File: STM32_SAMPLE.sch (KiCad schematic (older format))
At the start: 19 parts

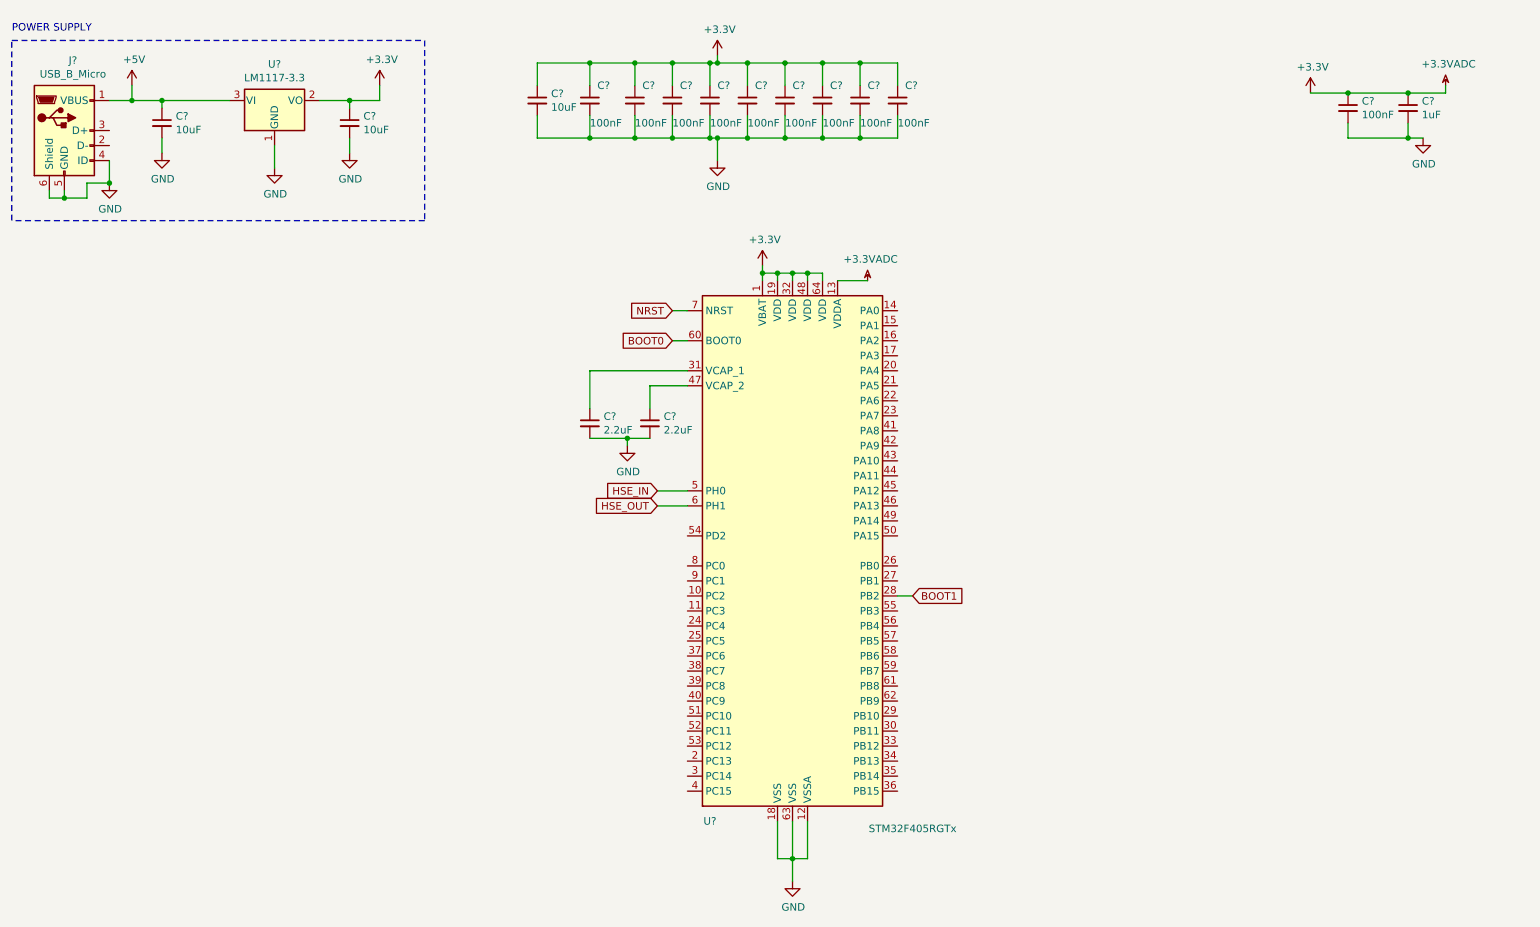
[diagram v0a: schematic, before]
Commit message: STM32 board bare minimum with HSI clock
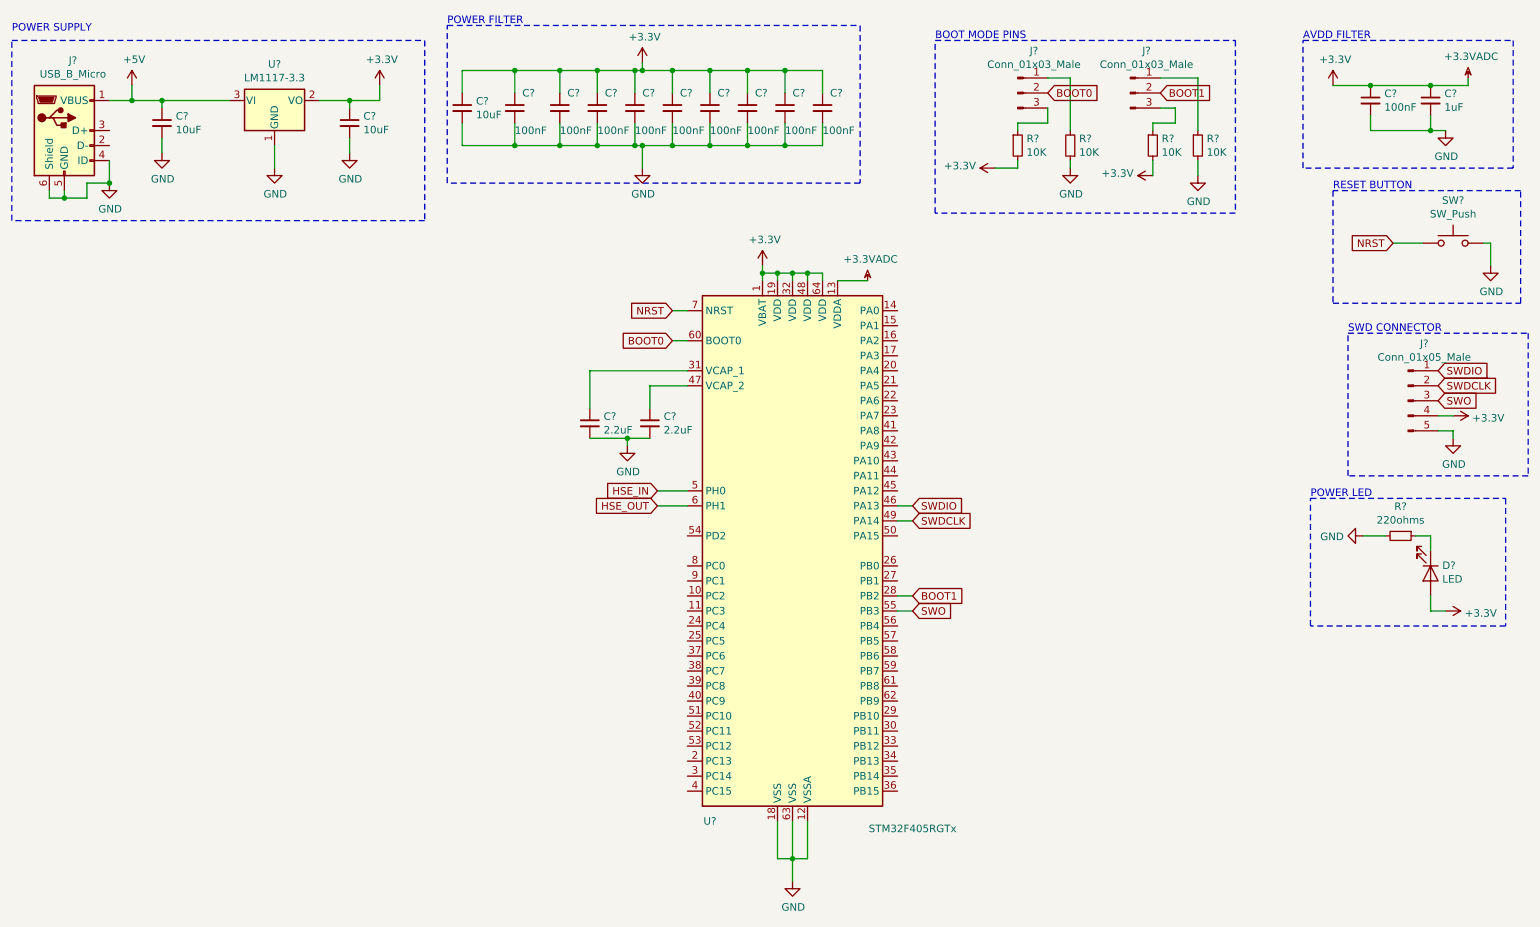
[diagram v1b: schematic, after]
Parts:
- added D?: LED, symbol Device:LED
- added J? (x2): Conn_01x03_Male, symbol Connector:Conn_01x03_Male
- added J?: Conn_01x05_Male, symbol Connector:Conn_01x05_Male
- added R? (x4): 10K, symbol Device:R_Small
- added R?: 220ohms, symbol Device:R_Small
- added SW?: SW_Push, symbol Switch:SW_Push
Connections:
- net +3.3VADC: now also D?.2 (A), J?.4 (Pin_4), R?.2, R?.2
- net BOOT0: now also J?.2 (Pin_2)
- net BOOT1: now also J?.2 (Pin_2)
- net GND: now also J?.5 (Pin_5), R?.1, R?.2, R?.2, SW?.2
- net NRST: now also SW?.1
- net SWDIO: now reaches U?.46 (PA13)
- net SWDIO: now also J?.1 (Pin_1)
- net SWDCLK: now reaches U?.49 (PA14)
- net SWDCLK: now also J?.2 (Pin_2)
- net SWO: now reaches U?.55 (PB3)
- net SWO: now also J?.3 (Pin_3)
- new net: J?.1 (Pin_1), R?.1
- new net: J?.3 (Pin_3), R?.1 (x2)
- new net: J?.1 (Pin_1), R?.2
- new net: D?.1 (K), R?.1
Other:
- note added: "AVDD FILTER"
- note added: "BOOT MODE PINS"
- note added: "POWER FILTER\n"
- note added: "POWER LED\n"
- note added: "RESET BUTTON\n"
- note added: "SWD CONNECTOR\n"
- moved on the sheet: C?
